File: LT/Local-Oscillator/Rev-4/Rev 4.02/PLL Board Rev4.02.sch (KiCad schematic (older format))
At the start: 69 parts, among them J1 Conn_01x02_Male, J13 Conn_01x02_Male, J14 Conn_01x02_Male, J15 Conn_01x02_Male, J16 Conn_01x02_Male, J17 Conn_01x02_Male, J18 Conn_Coaxial, J2 Conn_Coaxial, J20 Conn_01x02_Male, J3 Conn_Coaxial, J4 Conn_01x04_Male, J5 Conn_01x02_Male, J7 Conn_01x02_Male, J8 Conn_01x02_Male, Q1 2N5486 JFET, Q2 2N5486 JFET, U1 LMX231X, U2 L7808

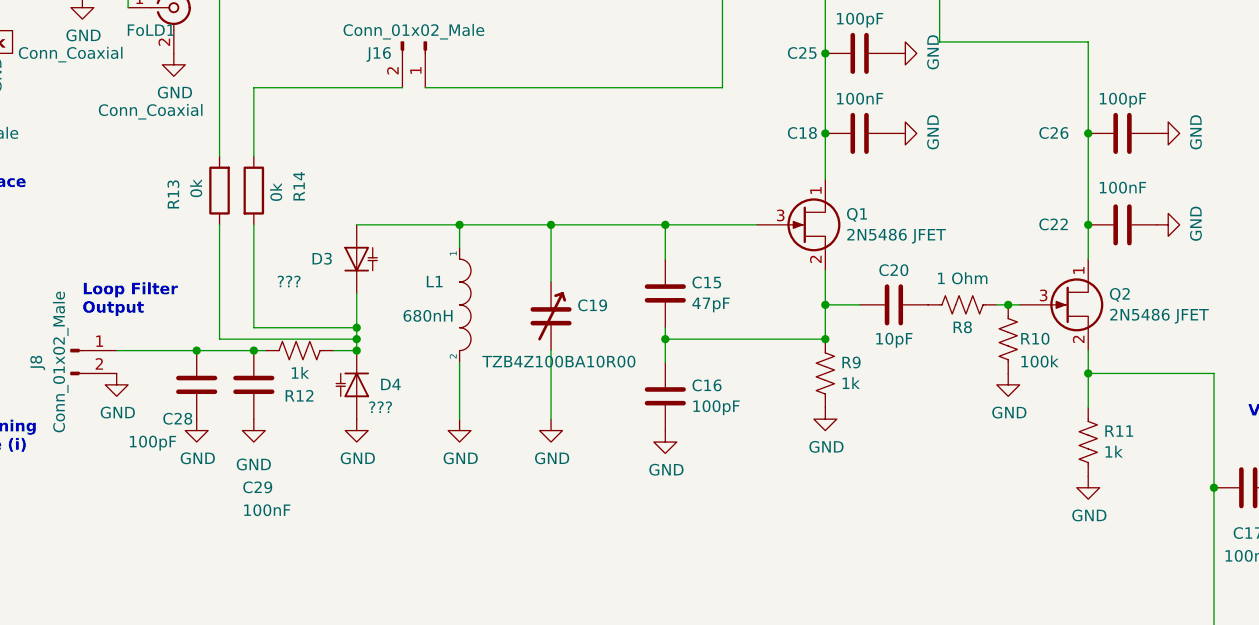
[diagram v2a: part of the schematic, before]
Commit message: Changed Resistor Symbols
Fixed the resistor symbols from PLL Rev 4.1-4.3
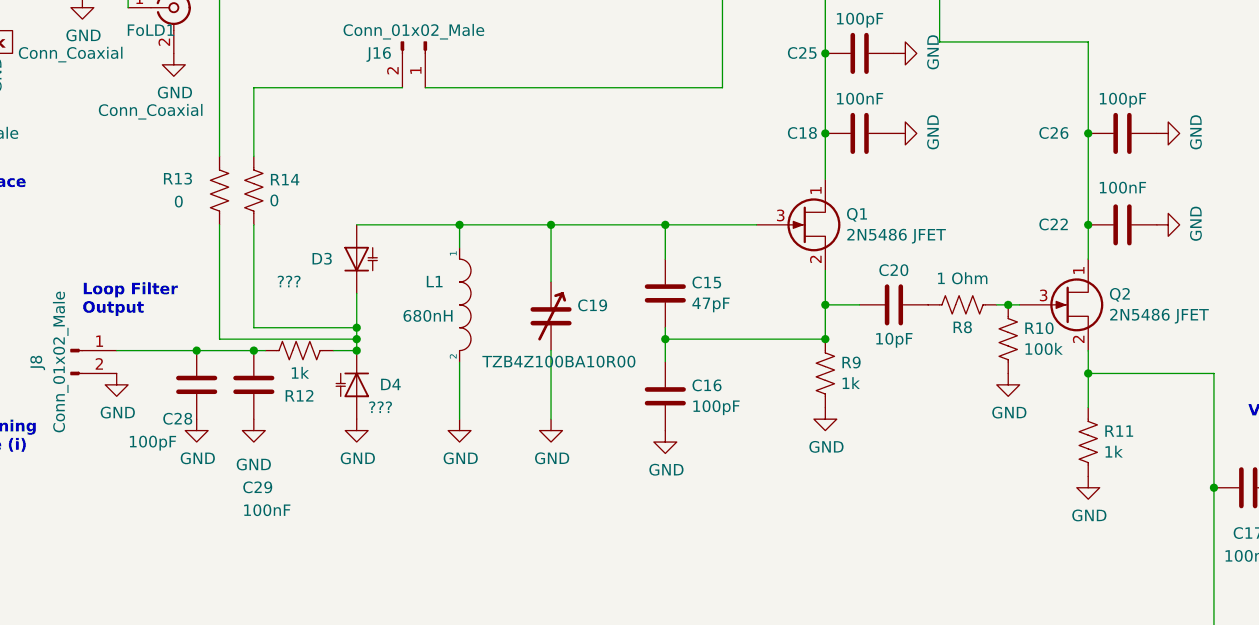
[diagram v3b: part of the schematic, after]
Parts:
- removed R1, R3, R4: 18, Resistor_SMD:R_0805_2012Metric_Pad1.15x1.40mm_HandSolder, symbol Device:R
- removed R10: 100k, Resistor_SMD:R_0805_2012Metric_Pad1.15x1.40mm_HandSolder, symbol Device:R
- removed R11, R12, R6, R9: 1k, Resistor_SMD:R_0805_2012Metric_Pad1.15x1.40mm_HandSolder, symbol Device:R
- removed R13, R14: 0k, Resistor_SMD:R_0805_2012Metric_Pad1.15x1.40mm_HandSolder, symbol PLL-Board-Rev4.02-rescue:R-Device-Complete-PLL-Board-Rev4-rescue-PLL-Board-Rev4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
- removed R2: 10k, Resistor_SMD:R_0805_2012Metric_Pad1.15x1.40mm_HandSolder, symbol Device:R
- removed R5: R, Resistor_SMD:R_0805_2012Metric_Pad1.15x1.40mm_HandSolder, symbol Device:R
- removed R7: 62k, Resistor_SMD:R_0805_2012Metric_Pad1.15x1.40mm_HandSolder, symbol Device:R
- removed R8: 1 Ohm, Resistor_SMD:R_0805_2012Metric_Pad1.15x1.40mm_HandSolder, symbol Device:R
- added R1, R3, R4: 18, Resistor_SMD:R_0805_2012Metric_Pad1.15x1.40mm_HandSolder, symbol Device:R_US
- added R10: 100k, Resistor_SMD:R_0805_2012Metric_Pad1.15x1.40mm_HandSolder, symbol Device:R_US
- added R11, R12, R6, R9: 1k, Resistor_SMD:R_0805_2012Metric_Pad1.15x1.40mm_HandSolder, symbol Device:R_US
- added R13, R14: 0, Resistor_SMD:R_0805_2012Metric_Pad1.15x1.40mm_HandSolder, symbol Device:R_US
- added R2: 10k, Resistor_SMD:R_0805_2012Metric_Pad1.15x1.40mm_HandSolder, symbol Device:R_US
- added R5: R, Resistor_SMD:R_0805_2012Metric_Pad1.15x1.40mm_HandSolder, symbol Device:R_US
- added R7: 62k, Resistor_SMD:R_0805_2012Metric_Pad1.15x1.40mm_HandSolder, symbol Device:R_US
- added R8: 1 Ohm, Resistor_SMD:R_0805_2012Metric_Pad1.15x1.40mm_HandSolder, symbol Device:R_US
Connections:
- net CE: now also R2.2
- net GND: now also R10.2, R11.1, R9.2
- net PLL_Power: now also R1.1, R2.1, R3.1, R4.1
- net V_uC: now also R1.2
- net Vcc: now also R3.2
- net Vp: now also R4.2
- net at C15.1, C16.2, C20.1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: now also R9.1
- net at D3.1 (K), D4.1 (K): now also R12.1, R13.2, R14.2
- net at C20.2: now also R8.2
- net at C13.1, J14.1 (Pin_1), J15.1 (Pin_1): now also R5.2
- net at C12.2, J13.1 (Pin_1): now also R6.2, R7.2
- net at C17.1, J7.1 (Pin_1), Q2.2 (S): now also R11.2
- net at Q2.3 (G): now also R10.1, R8.1
- net at J15.2 (Pin_2): now also R13.1
- net at C28.2, C29.2, J8.1 (Pin_1): now also R12.2
- net at C14.1: now also R5.1
- net at C24.1, J16.1 (Pin_1): now also R6.1
- net at J16.2 (Pin_2): now also R14.1
- net at C23.1: now also R7.1
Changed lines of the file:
@@
 Wire Wire Line
 	8800 4900 8950 4900
-$Comp
-L PLL-Board-Rev4.02-rescue:R-Device-Complete-PLL-Board-Rev4-rescue-PLL-Board-Rev4.01-rescue R13
-U 1 1 5CBB0D39
-P 6150 4400
-F 0 "R13" V 6350 4350 50  0000 L CNN
-F 1 "0k" V 6250 4350 50  0000 L CNN
-F 2 "Resistor_SMD:R_0805_2012Metric_Pad1.15x1.40mm_HandSolder" V 6080 4400 50  0001 C CNN
-F 3 "~" H 6150 4400 50  0001 C CNN
-	1    6150 4400
-	-1   0    0    1
-$EndComp
-$Comp
-L PLL-Board-Rev4.02-rescue:R-Device-Complete-PLL-Board-Rev4-rescue-PLL-Board-Rev4.01-rescue R14
-U 1 1 5CBBAAF0
-P 6300 4400
-F 0 "R14" V 6500 4350 50  0000 L CNN
-F 1 "0k" V 6400 4350 50  0000 L CNN
-F 2 "Resistor_SMD:R_0805_2012Metric_Pad1.15x1.40mm_HandSolder" V 6230 4400 50  0001 C CNN
-F 3 "~" H 6300 4400 50  0001 C CNN
-	1    6300 4400
-	1    0    0    -1
-$EndComp
 Wire Wire Line
 	6300 3950 6300 4250
@@
 Rev4.02: Unknown Varactor Values
 $Comp
-L Device:R R1
-U 1 1 5E5BE92F
+L Device:R_US R1
+U 1 1 5E646F83
 P 2500 1400
 F 0 "R1" H 2568 1446 50  0000 L CNN
@@
 $EndComp
 $Comp
-L Device:R R2
-U 1 1 5E5CF74D
+L Device:R_US R3
+U 1 1 5E64C888
+P 3500 1350
+F 0 "R3" H 3568 1396 50  0000 L CNN
+F 1 "18" H 3568 1305 50  0000 L CNN
+F 2 "Resistor_SMD:R_0805_2012Metric_Pad1.15x1.40mm_HandSolder" V 3540 1340 50  0001 C CNN
+F 3 "~" H 3500 1350 50  0001 C CNN
+	1    3500 1350
+	1    0    0    -1
+$EndComp
+$Comp
+L Device:R_US R4
+U 1 1 5E64D112
+P 4000 1350
+F 0 "R4" H 4068 1396 50  0000 L CNN
+F 1 "18" H 4068 1305 50  0000 L CNN
+F 2 "Resistor_SMD:R_0805_2012Metric_Pad1.15x1.40mm_HandSolder" V 4040 1340 50  0001 C CNN
+F 3 "~" H 4000 1350 50  0001 C CNN
+	1    4000 1350
+	1    0    0    -1
+$EndComp
+Connection ~ 3500 1500
+$Comp
+L Device:R_US R2
+U 1 1 5E656741
 P 2800 2100
 F 0 "R2" H 2868 2146 50  0000 L CNN
@@
 $EndComp
 $Comp
-L Device:R R3
-U 1 1 5E5D8387
-P 3500 1350
-F 0 "R3" H 3568 1396 50  0000 L CNN
-F 1 "18" H 3568 1305 50  0000 L CNN
-F 2 "Resistor_SMD:R_0805_2012Metric_Pad1.15x1.40mm_HandSolder" V 3540 1340 50  0001 C CNN
-F 3 "~" H 3500 1350 50  0001 C CNN
-	1    3500 1350
-	1    0    0    -1
-$EndComp
-Connection ~ 3500 1500
-$Comp
-L Device:R R4
-U 1 1 5E602E93
-P 4000 1350
-F 0 "R4" H 4068 1396 50  0000 L CNN
-F 1 "18" H 4068 1305 50  0000 L CNN
-F 2 "Resistor_SMD:R_0805_2012Metric_Pad1.15x1.40mm_HandSolder" V 4040 1340 50  0001 C CNN
-F 3 "~" H 4000 1350 50  0001 C CNN
-	1    4000 1350
-	1    0    0    -1
-$EndComp
-$Comp
-L Device:R R7
-U 1 1 5E60981A
+L Device:R_US R13
+U 1 1 5E65C4D0
+P 6150 4400
+F 0 "R13" H 5900 4450 50  0000 L CNN
+F 1 "0" H 5950 4350 50  0000 L CNN
+F 2 "Resistor_SMD:R_0805_2012Metric_Pad1.15x1.40mm_HandSolder" V 6190 4390 50  0001 C CNN
+F 3 "~" H 6150 4400 50  0001 C CNN
+	1    6150 4400
+	1    0    0    -1
+$EndComp
+$Comp
+L Device:R_US R14
+U 1 1 5E65D5DF
+P 6300 4400
+F 0 "R14" H 6368 4446 50  0000 L CNN
+F 1 "0" H 6368 4355 50  0000 L CNN
+F 2 "Resistor_SMD:R_0805_2012Metric_Pad1.15x1.40mm_HandSolder" V 6340 4390 50  0001 C CNN
+F 3 "~" H 6300 4400 50  0001 C CNN
+	1    6300 4400
+	1    0    0    -1
+$EndComp
+$Comp
+L Device:R_US R12
+U 1 1 5E668D88
+P 6500 5100
+F 0 "R12" V 6700 5100 50  0000 C CNN
+F 1 "1k" V 6600 5100 50  0000 C CNN
+F 2 "Resistor_SMD:R_0805_2012Metric_Pad1.15x1.40mm_HandSolder" V 6540 5090 50  0001 C CNN
+F 3 "~" H 6500 5100 50  0001 C CNN
+	1    6500 5100
+	0    1    1    0
+$EndComp
+$Comp
+L Device:R_US R9
+U 1 1 5E67154C
+P 8800 5200
+F 0 "R9" H 8868 5246 50  0000 L CNN
+F 1 "1k" H 8868 5155 50  0000 L CNN
+F 2 "Resistor_SMD:R_0805_2012Metric_Pad1.15x1.40mm_HandSolder" V 8840 5190 50  0001 C CNN
+F 3 "~" H 8800 5200 50  0001 C CNN
+	1    8800 5200
+	1    0    0    -1
+$EndComp
+Connection ~ 8800 5050
+$Comp
+L Device:R_US R10
+U 1 1 5E6770BB
+P 9600 5050
+F 0 "R10" H 9668 5096 50  0000 L CNN
+F 1 "100k" H 9668 5005 50  0000 L CNN
+F 2 "Resistor_SMD:R_0805_2012Metric_Pad1.15x1.40mm_HandSolder" V 9640 5040 50  0001 C CNN
+F 3 "~" H 9600 5050 50  0001 C CNN
+	1    9600 5050
+	1    0    0    -1
+$EndComp
+Wire Wire Line
+	9550 4900 9600 4900
+Connection ~ 9600 4900
+Wire Wire Line
+	9600 4900 9650 4900
+$Comp
+L Device:R_US R8
+U 1 1 5E67C89E
+P 9400 4900
+F 0 "R8" V 9500 4900 50  0000 C CNN
+F 1 "1 Ohm" V 9286 4900 50  0000 C CNN
+F 2 "Resistor_SMD:R_0805_2012Metric_Pad1.15x1.40mm_HandSolder" V 9440 4890 50  0001 C CNN
+F 3 "~" H 9400 4900 50  0001 C CNN
+	1    9400 4900
+	0    1    1    0
+$EndComp
+$Comp
+L Device:R_US R11
+U 1 1 5E682531
+P 9950 5500
+F 0 "R11" H 9882 5454 50  0000 R CNN
+F 1 "1k" H 9882 5545 50  0000 R CNN
+F 2 "Resistor_SMD:R_0805_2012Metric_Pad1.15x1.40mm_HandSolder" V 9990 5490 50  0001 C CNN
+F 3 "~" H 9950 5500 50  0001 C CNN
+	1    9950 5500
+	-1   0    0    1
+$EndComp
+$Comp
+L Device:R_US R5
+U 1 1 5E687F64
+P 7500 2850
+F 0 "R5" H 7568 2896 50  0000 L CNN
+F 1 "R" H 7568 2805 50  0000 L CNN
+F 2 "Resistor_SMD:R_0805_2012Metric_Pad1.15x1.40mm_HandSolder" V 7540 2840 50  0001 C CNN
+F 3 "~" H 7500 2850 50  0001 C CNN
+	1    7500 2850
+	1    0    0    -1
+$EndComp
+Wire Wire Line
+	6950 3000 7500 3000
+Connection ~ 7500 3000
+Wire Wire Line
+	7500 3000 7800 3000
+$Comp
+L Device:R_US R7
+U 1 1 5E68E0A4
 P 7550 1300
 F 0 "R7" H 7618 1346 50  0000 L CNN
@@
 $EndComp
 $Comp
-L Device:R R6
-U 1 1 5E61214C
+L Device:R_US R6
+U 1 1 5E6950A9
 P 7700 1850
 F 0 "R6" V 7495 1850 50  0000 C CNN
@@
 $EndComp
 Connection ~ 7550 1850
-Wire Wire Line
-	6950 3000 7500 3000
-$Comp
-L Device:R R5
-U 1 1 5E62005C
-P 7500 2850
-F 0 "R5" H 7568 2896 50  0000 L CNN
-F 1 "R" H 7568 2805 50  0000 L CNN
-F 2 "Resistor_SMD:R_0805_2012Metric_Pad1.15x1.40mm_HandSolder" V 7540 2840 50  0001 C CNN
-F 3 "~" H 7500 2850 50  0001 C CNN
-	1    7500 2850
-	1    0    0    -1
-$EndComp
-Connection ~ 7500 3000
-Wire Wire Line
-	7500 3000 7800 3000
-$Comp
-L Device:R R12
-U 1 1 5E6214BA
-P 6500 5100
-F 0 "R12" V 6700 5100 50  0000 C CNN
-F 1 "1k" V 6600 5100 50  0000 C CNN
-F 2 "Resistor_SMD:R_0805_2012Metric_Pad1.15x1.40mm_HandSolder" V 6540 5090 50  0001 C CNN
-F 3 "~" H 6500 5100 50  0001 C CNN
-	1    6500 5100
-	0    1    1    0
-$EndComp
-$Comp
-L Device:R R9
-U 1 1 5E62803C
-P 8800 5200
-F 0 "R9" H 8868 5246 50  0000 L CNN
-F 1 "1k" H 8868 5155 50  0000 L CNN
-F 2 "Resistor_SMD:R_0805_2012Metric_Pad1.15x1.40mm_HandSolder" V 8840 5190 50  0001 C CNN
-F 3 "~" H 8800 5200 50  0001 C CNN
-	1    8800 5200
-	1    0    0    -1
-$EndComp
-Connection ~ 8800 5050
-$Comp
-L Device:R R8
-U 1 1 5E62E4C4
-P 9400 4900
-F 0 "R8" V 9500 4900 50  0000 C CNN
-F 1 "1 Ohm" V 9286 4900 50  0000 C CNN
-F 2 "Resistor_SMD:R_0805_2012Metric_Pad1.15x1.40mm_HandSolder" V 9440 4890 50  0001 C CNN
-F 3 "~" H 9400 4900 50  0001 C CNN
-	1    9400 4900
-	0    1    1    0
-$EndComp
-$Comp
-L Device:R R10
-U 1 1 5E63424F
-P 9600 5050
-F 0 "R10" H 9650 5050 50  0000 L CNN
-F 1 "100k" H 9650 4950 50  0000 L CNN
-F 2 "Resistor_SMD:R_0805_2012Metric_Pad1.15x1.40mm_HandSolder" V 9640 5040 50  0001 C CNN
-F 3 "~" H 9600 5050 50  0001 C CNN
-	1    9600 5050
-	1    0    0    -1
-$EndComp
-Wire Wire Line
-	9550 4900 9600 4900
-Connection ~ 9600 4900
-Wire Wire Line
-	9600 4900 9650 4900
-$Comp
-L Device:R R11
-U 1 1 5E63AEDD
-P 9950 5500
-F 0 "R11" H 10018 5546 50  0000 L CNN
-F 1 "1k" H 10018 5455 50  0000 L CNN
-F 2 "Resistor_SMD:R_0805_2012Metric_Pad1.15x1.40mm_HandSolder" V 9990 5490 50  0001 C CNN
-F 3 "~" H 9950 5500 50  0001 C CNN
-	1    9950 5500
-	1    0    0    -1
-$EndComp
 $EndSCHEMATC
